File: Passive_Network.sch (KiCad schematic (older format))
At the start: 148 parts, among them J18 CONN_01X03, J19 CONN_01X03, J20 CONN_01X08, SW2 SW_Rotary3x4, X1 P7002SCLRP, X2 P7002SCLRP, X3 P7002SCLRP, X4 P7002SCLRP, X5 P7002SCLRP, X6 P7002SCLRP

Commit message: 2차PCB
U22 포함
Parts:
- R14: footprint Resistors_SMD:R_0805_HandSoldering -> Resistors_SMD:R_1206_HandSoldering
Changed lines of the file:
@@
 F 0 "R14" V 4000 3800 50  0000 C CNN
 F 1 "10k" V 3950 3600 50  0000 C CNN
-F 2 "Resistors_SMD:R_0805_HandSoldering" V 3880 3600 50  0001 C CNN
+F 2 "Resistors_SMD:R_1206_HandSoldering" V 3880 3600 50  0001 C CNN
 F 3 "" H 3950 3600 50  0001 C CNN
 	1    3950 3600

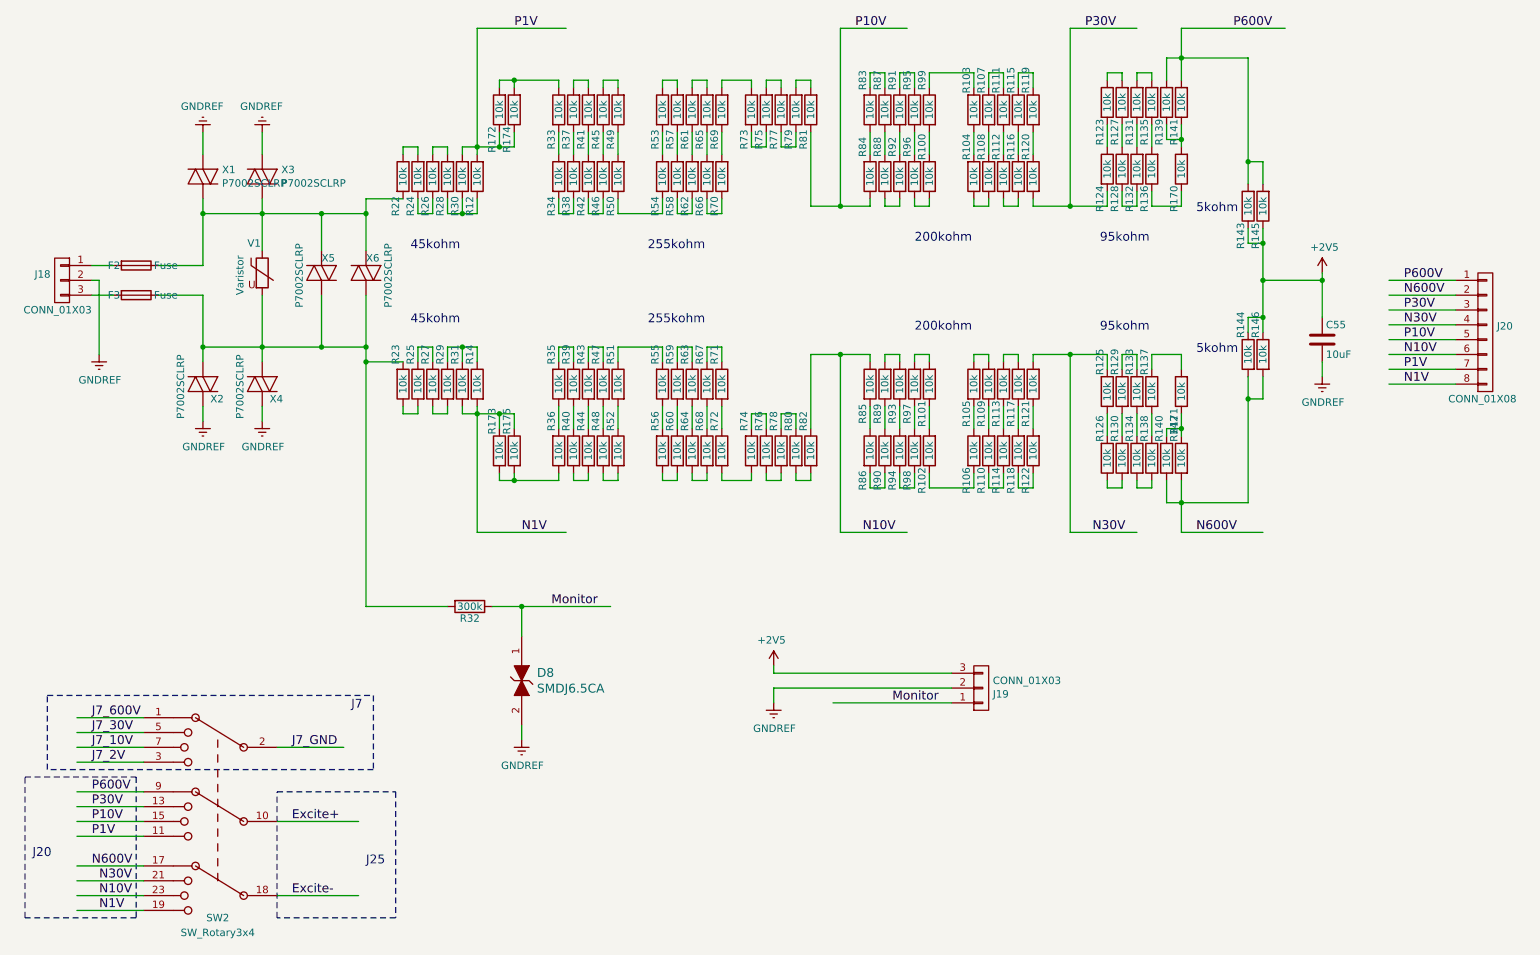
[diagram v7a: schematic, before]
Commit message: High Voltage reinforce
고전압 부분 보강
AN2, AN3 두 부분 6.5V limit
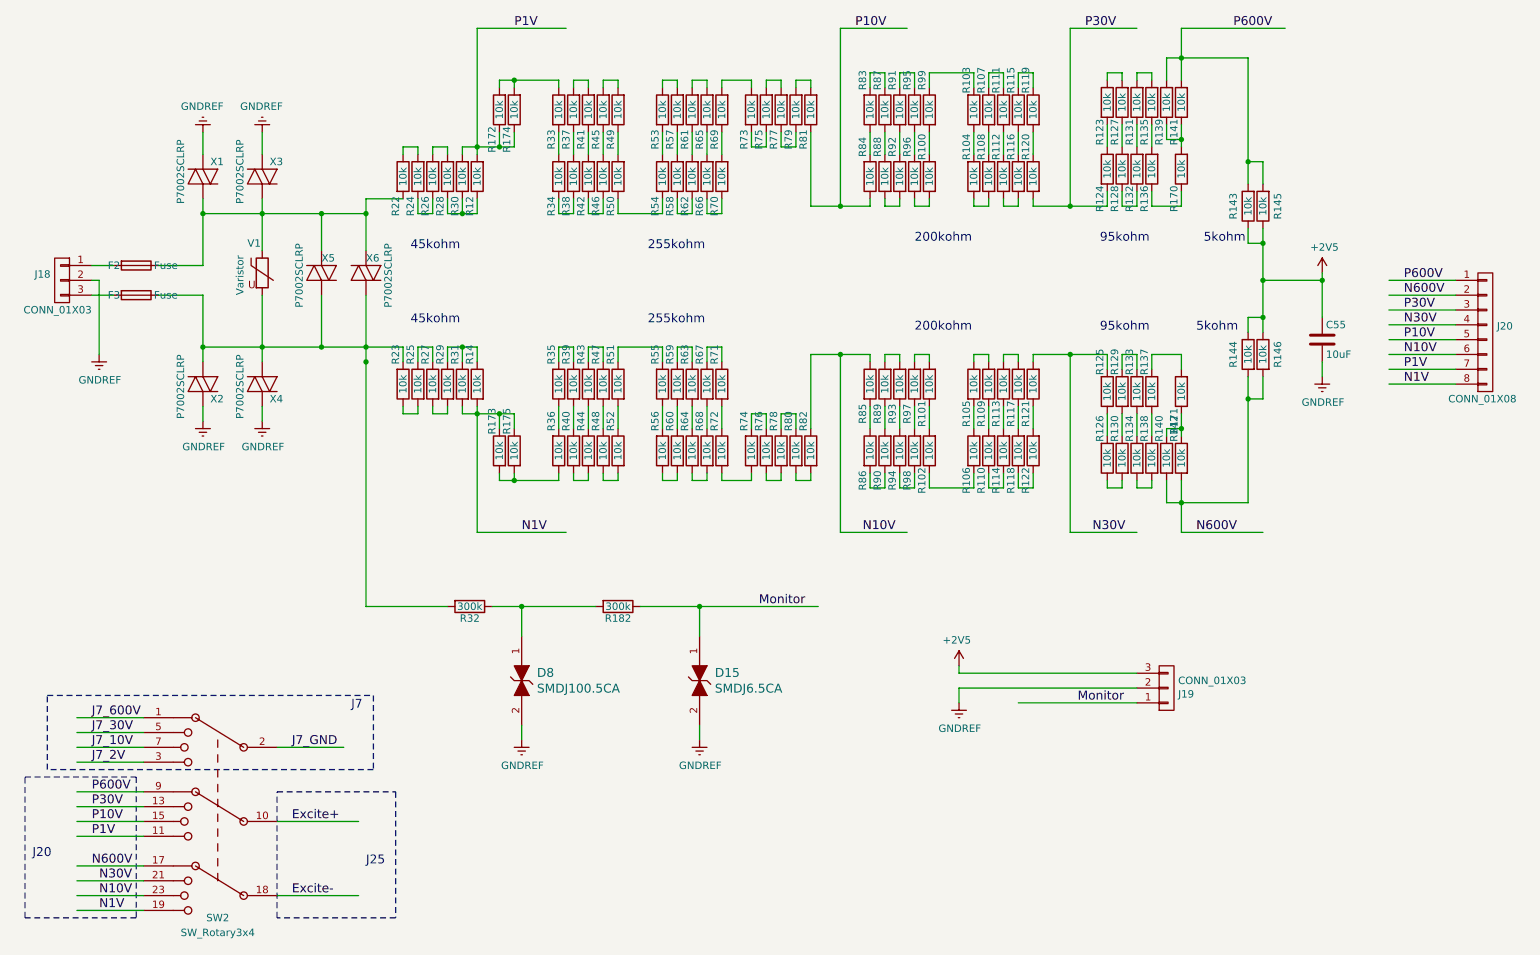
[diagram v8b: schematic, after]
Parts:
- added D15: SMDJ6.5CA, Diodes_SMD:D_SMC_Handsoldering, symbol PGB1010603MR
- added R182: 300k, Resistors_THT:R_Axial_Power_L20.0mm_W6.4mm_P22.40mm, symbol R
- D8: value SMDJ6.5CA -> SMDJ100.5CA
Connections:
- wire segments 358 -> 361
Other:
- moved on the sheet: J19
